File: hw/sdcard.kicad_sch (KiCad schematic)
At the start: 5 parts, among them J2401 MSD-1-A, U2401 CM1624

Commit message: Starting to switch to new rx architecture
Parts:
- renumbered C2401 to C2701, C2402 to C2702, J2401 to J2701, R2401 to R2701, U2401 to U2701
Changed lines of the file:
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@@
 		(dnp no)
 		(fields_autoplaced yes)
-		(property "Reference" "#PWR02401"
+		(property "Reference" "#PWR02701"
 			(at 71.12 102.87 0)
 			(effects
@@
 			(project "USB-SSB-txcvr"
 				(path "/8ae46c04-d01a-4756-8774-512b694bfaff/c32f5700-dc71-4705-afb9-ca83a93b0543/ec3731a3-df09-4e93-b25b-76297aeb30bb"
-					(reference "#PWR02401")
+					(reference "#PWR02701")
 					(unit 1)
 				)
@@
 		(on_board yes)
 		(dnp no)
-		(property "Reference" "U2401"
+		(property "Reference" "U2701"
 			(at 68.9767 57.15 0)
 			(effects
@@
 			(project "USB-SSB-txcvr"
 				(path "/8ae46c04-d01a-4756-8774-512b694bfaff/c32f5700-dc71-4705-afb9-ca83a93b0543/ec3731a3-df09-4e93-b25b-76297aeb30bb"
-					(reference "U2401")
+					(reference "U2701")
 					(unit 1)
 				)
@@
 		(dnp no)
 		(fields_autoplaced yes)
-		(property "Reference" "#PWR02405"
+		(property "Reference" "#PWR02705"
 			(at 185.42 67.31 0)
 			(effects
@@
 			(project ""
 				(path "/8ae46c04-d01a-4756-8774-512b694bfaff/c32f5700-dc71-4705-afb9-ca83a93b0543/ec3731a3-df09-4e93-b25b-76297aeb30bb"
-					(reference "#PWR02405")
+					(reference "#PWR02705")
 					(unit 1)
 				)
@@
 		(dnp no)
 		(fields_autoplaced yes)
-		(property "Reference" "J2401"
+		(property "Reference" "J2701"
 			(at 154.94 63.5 0)
 			(effects
@@
 			(project ""
 				(path "/8ae46c04-d01a-4756-8774-512b694bfaff/c32f5700-dc71-4705-afb9-ca83a93b0543/ec3731a3-df09-4e93-b25b-76297aeb30bb"
-					(reference "J2401")
+					(reference "J2701")
 					(unit 1)
 				)
@@
 		(on_board yes)
 		(dnp no)
-		(property "Reference" "C2402"
+		(property "Reference" "C2702"
 			(at 116.078 78.994 0)
 			(effects
@@
 			(project ""
 				(path "/8ae46c04-d01a-4756-8774-512b694bfaff/c32f5700-dc71-4705-afb9-ca83a93b0543/ec3731a3-df09-4e93-b25b-76297aeb30bb"
-					(reference "C2402")
+					(reference "C2702")
 					(unit 1)
 				)
@@
 		(dnp no)
 		(fields_autoplaced yes)
-		(property "Reference" "#PWR02403"
+		(property "Reference" "#PWR02703"
 			(at 124.46 99.06 0)
 			(effects
@@
 			(project "USB-SSB-txcvr"
 				(path "/8ae46c04-d01a-4756-8774-512b694bfaff/c32f5700-dc71-4705-afb9-ca83a93b0543/ec3731a3-df09-4e93-b25b-76297aeb30bb"
-					(reference "#PWR02403")
+					(reference "#PWR02703")
 					(unit 1)
 				)
@@
 		(on_board yes)
 		(dnp no)
-		(property "Reference" "#PWR02402"
+		(property "Reference" "#PWR02702"
 			(at 124.46 68.58 0)
 			(effects
@@
 			(project "USB-SSB-txcvr"
 				(path "/8ae46c04-d01a-4756-8774-512b694bfaff/c32f5700-dc71-4705-afb9-ca83a93b0543/ec3731a3-df09-4e93-b25b-76297aeb30bb"
-					(reference "#PWR02402")
+					(reference "#PWR02702")
 					(unit 1)
 				)
@@
 		(dnp no)
 		(fields_autoplaced yes)
-		(property "Reference" "#PWR02404"
+		(property "Reference" "#PWR02704"
 			(at 175.26 81.28 0)
 			(effects
@@
 			(project ""
 				(path "/8ae46c04-d01a-4756-8774-512b694bfaff/c32f5700-dc71-4705-afb9-ca83a93b0543/ec3731a3-df09-4e93-b25b-76297aeb30bb"
-					(reference "#PWR02404")
+					(reference "#PWR02704")
 					(unit 1)
 				)
@@
 		(on_board yes)
 		(dnp no)
-		(property "Reference" "C2401"
+		(property "Reference" "C2701"
 			(at 108.458 78.994 0)
 			(effects
@@
 			(project "USB-SSB-txcvr"
 				(path "/8ae46c04-d01a-4756-8774-512b694bfaff/c32f5700-dc71-4705-afb9-ca83a93b0543/ec3731a3-df09-4e93-b25b-76297aeb30bb"
-					(reference "C2401")
+					(reference "C2701")
 					(unit 1)
 				)
@@
 		(dnp no)
 		(fields_autoplaced yes)
-		(property "Reference" "R2401"
+		(property "Reference" "R2701"
 			(at 187.96 77.4699 0)
 			(effects
@@
 			(project ""
 				(path "/8ae46c04-d01a-4756-8774-512b694bfaff/c32f5700-dc71-4705-afb9-ca83a93b0543/ec3731a3-df09-4e93-b25b-76297aeb30bb"
-					(reference "R2401")
+					(reference "R2701")
 					(unit 1)
 				)

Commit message: Converting to use busses as global symbols instead of tedium. Using 2n7002 Nexperia dual MOSFET because of its LOW LOW capacitance spec for L, C, and attenuator switching.
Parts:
- renumbered C2701 to C2401, C2702 to C2402, J2701 to J2401, R2701 to R2401, U2701 to U2401
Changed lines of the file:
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@@
 		(dnp no)
 		(fields_autoplaced yes)
-		(property "Reference" "#PWR02701"
+		(property "Reference" "#PWR02401"
 			(at 71.12 102.87 0)
 			(effects
@@
 					(size 1.27 1.27)
 				)
+				(hide yes)
 			)
 		)
@@
 			(project "USB-SSB-txcvr"
 				(path "/8ae46c04-d01a-4756-8774-512b694bfaff/c32f5700-dc71-4705-afb9-ca83a93b0543/ec3731a3-df09-4e93-b25b-76297aeb30bb"
-					(reference "#PWR02701")
+					(reference "#PWR02401")
 					(unit 1)
 				)
@@
 		(on_board yes)
 		(dnp no)
-		(property "Reference" "U2701"
+		(property "Reference" "U2401"
 			(at 68.9767 57.15 0)
 			(effects
@@
 			(project "USB-SSB-txcvr"
 				(path "/8ae46c04-d01a-4756-8774-512b694bfaff/c32f5700-dc71-4705-afb9-ca83a93b0543/ec3731a3-df09-4e93-b25b-76297aeb30bb"
-					(reference "U2701")
+					(reference "U2401")
 					(unit 1)
 				)
@@
 		(dnp no)
 		(fields_autoplaced yes)
-		(property "Reference" "#PWR02705"
+		(property "Reference" "#PWR02405"
 			(at 185.42 67.31 0)
 			(effects
@@
 			(project ""
 				(path "/8ae46c04-d01a-4756-8774-512b694bfaff/c32f5700-dc71-4705-afb9-ca83a93b0543/ec3731a3-df09-4e93-b25b-76297aeb30bb"
-					(reference "#PWR02705")
+					(reference "#PWR02405")
 					(unit 1)
 				)
@@
 		(dnp no)
 		(fields_autoplaced yes)
-		(property "Reference" "J2701"
+		(property "Reference" "J2401"
 			(at 154.94 63.5 0)
 			(effects
@@
 			(project ""
 				(path "/8ae46c04-d01a-4756-8774-512b694bfaff/c32f5700-dc71-4705-afb9-ca83a93b0543/ec3731a3-df09-4e93-b25b-76297aeb30bb"
-					(reference "J2701")
+					(reference "J2401")
 					(unit 1)
 				)
@@
 		(on_board yes)
 		(dnp no)
-		(property "Reference" "C2702"
+		(property "Reference" "C2402"
 			(at 116.078 78.994 0)
 			(effects
@@
 			(project ""
 				(path "/8ae46c04-d01a-4756-8774-512b694bfaff/c32f5700-dc71-4705-afb9-ca83a93b0543/ec3731a3-df09-4e93-b25b-76297aeb30bb"
-					(reference "C2702")
+					(reference "C2402")
 					(unit 1)
 				)
@@
 		(dnp no)
 		(fields_autoplaced yes)
-		(property "Reference" "#PWR02703"
+		(property "Reference" "#PWR02403"
 			(at 124.46 99.06 0)
 			(effects
@@
 					(size 1.27 1.27)
 				)
+				(hide yes)
 			)
 		)
@@
 			(project "USB-SSB-txcvr"
 				(path "/8ae46c04-d01a-4756-8774-512b694bfaff/c32f5700-dc71-4705-afb9-ca83a93b0543/ec3731a3-df09-4e93-b25b-76297aeb30bb"
-					(reference "#PWR02703")
+					(reference "#PWR02403")
 					(unit 1)
 				)
@@
 		(on_board yes)
 		(dnp no)
-		(property "Reference" "#PWR02702"
+		(property "Reference" "#PWR02402"
 			(at 124.46 68.58 0)
 			(effects
@@
 			(project "USB-SSB-txcvr"
 				(path "/8ae46c04-d01a-4756-8774-512b694bfaff/c32f5700-dc71-4705-afb9-ca83a93b0543/ec3731a3-df09-4e93-b25b-76297aeb30bb"
-					(reference "#PWR02702")
+					(reference "#PWR02402")
 					(unit 1)
 				)
@@
 		(dnp no)
 		(fields_autoplaced yes)
-		(property "Reference" "#PWR02704"
+		(property "Reference" "#PWR02404"
 			(at 175.26 81.28 0)
 			(effects
@@
 			(project ""
 				(path "/8ae46c04-d01a-4756-8774-512b694bfaff/c32f5700-dc71-4705-afb9-ca83a93b0543/ec3731a3-df09-4e93-b25b-76297aeb30bb"
-					(reference "#PWR02704")
+					(reference "#PWR02404")
 					(unit 1)
 				)
@@
 		(on_board yes)
 		(dnp no)
-		(property "Reference" "C2701"
+		(property "Reference" "C2401"
 			(at 108.458 78.994 0)
 			(effects
@@
 			(project "USB-SSB-txcvr"
 				(path "/8ae46c04-d01a-4756-8774-512b694bfaff/c32f5700-dc71-4705-afb9-ca83a93b0543/ec3731a3-df09-4e93-b25b-76297aeb30bb"
-					(reference "C2701")
+					(reference "C2401")
 					(unit 1)
 				)
@@
 		(dnp no)
 		(fields_autoplaced yes)
-		(property "Reference" "R2701"
+		(property "Reference" "R2401"
 			(at 187.96 77.4699 0)
 			(effects
@@
 			(project ""
 				(path "/8ae46c04-d01a-4756-8774-512b694bfaff/c32f5700-dc71-4705-afb9-ca83a93b0543/ec3731a3-df09-4e93-b25b-76297aeb30bb"
-					(reference "R2701")
+					(reference "R2401")
 					(unit 1)
 				)

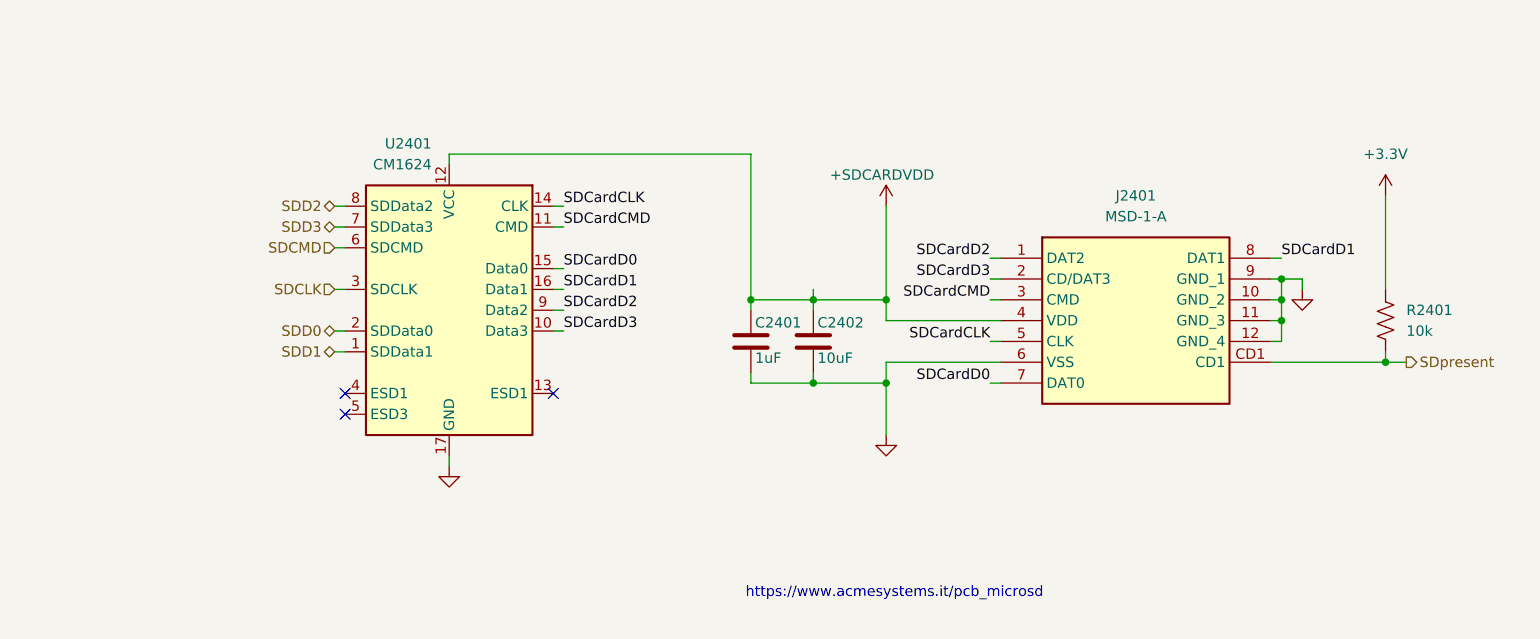
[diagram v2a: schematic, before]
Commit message: Added SD card ESD zap
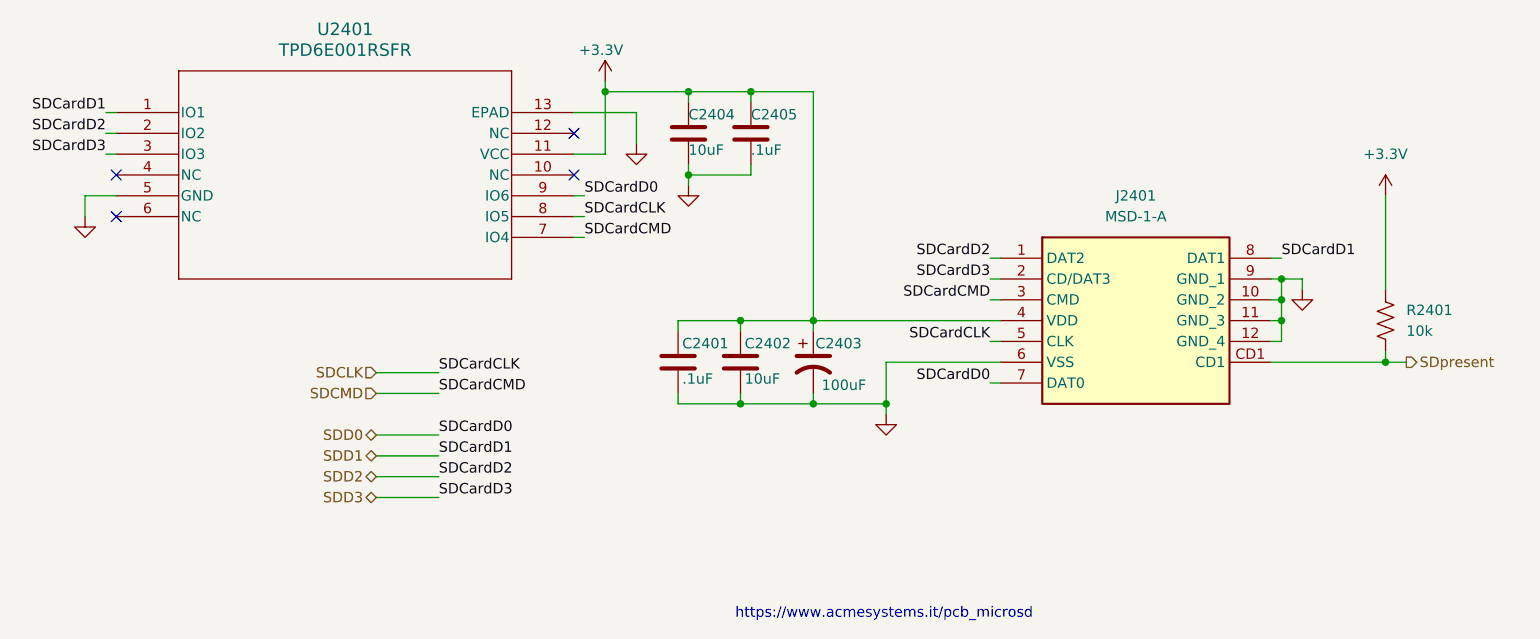
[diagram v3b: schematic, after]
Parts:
- removed U2401: CM1624, Package_DFN_QFN:OnSemi_UDFN-16-1EP_1.35x3.3mm_P0.4mm_EP0.4x2.8mm, symbol Power_Protection:CM1624
- added C2403: 100uF, symbol Device:C_Polarized_US
- added C2404: 10uF, Capacitor_SMD:C_0805_2012Metric, symbol Device:C
- added C2405: .1uF, Capacitor_SMD:C_0805_2012Metric, symbol Device:C
- added U2401: TPD6E001RSFR, RSF12_2P1X2P1, symbol TPD6E001RSFR:TPD6E001RSFR
- C2401: value 1uF -> .1uF
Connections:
- net +SDCARDVDD is gone; now on net +3.3V: C2401.1, C2402.1, J2401.4 (VDD)
- net SDCardCLK is gone; now on net SDCLK: J2401.5 (CLK)
- net SDCardCMD is gone; now on net SDCMD: J2401.3 (CMD)
- net SDCardD0 is gone; now on net SDD0: J2401.7 (DAT0)
- net SDCardD1 is gone; now on net SDD1: J2401.8 (DAT1)
- net SDCardD2 is gone; now on net SDD2: J2401.1 (DAT2)
- net SDCardD3 is gone; now on net SDD3: J2401.2 (CD/DAT3)
- net +3.3V: now also C2403.1, C2404.1, C2405.1, U2401.11 (VCC)
- net GND: now also C2403.2, C2404.2, C2405.2, U2401.13 (EPAD), U2401.5 (GND)
- net SDCLK: now also U2401.8 (IO5)
- net SDCMD: now also U2401.7 (IO4)
- net SDD0: now also U2401.9 (IO6)
- net SDD1: now also U2401.1 (IO1)
- net SDD2: now also U2401.2 (IO2)
- net SDD3: now also U2401.3 (IO3)
- no-connect marks 3 -> 4
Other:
- moved on the sheet: C2401, C2402

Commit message: Moved ant page into tx page, added Bruene Direction Coupler to measure VSWR. General cleanup, page renumber, reannote
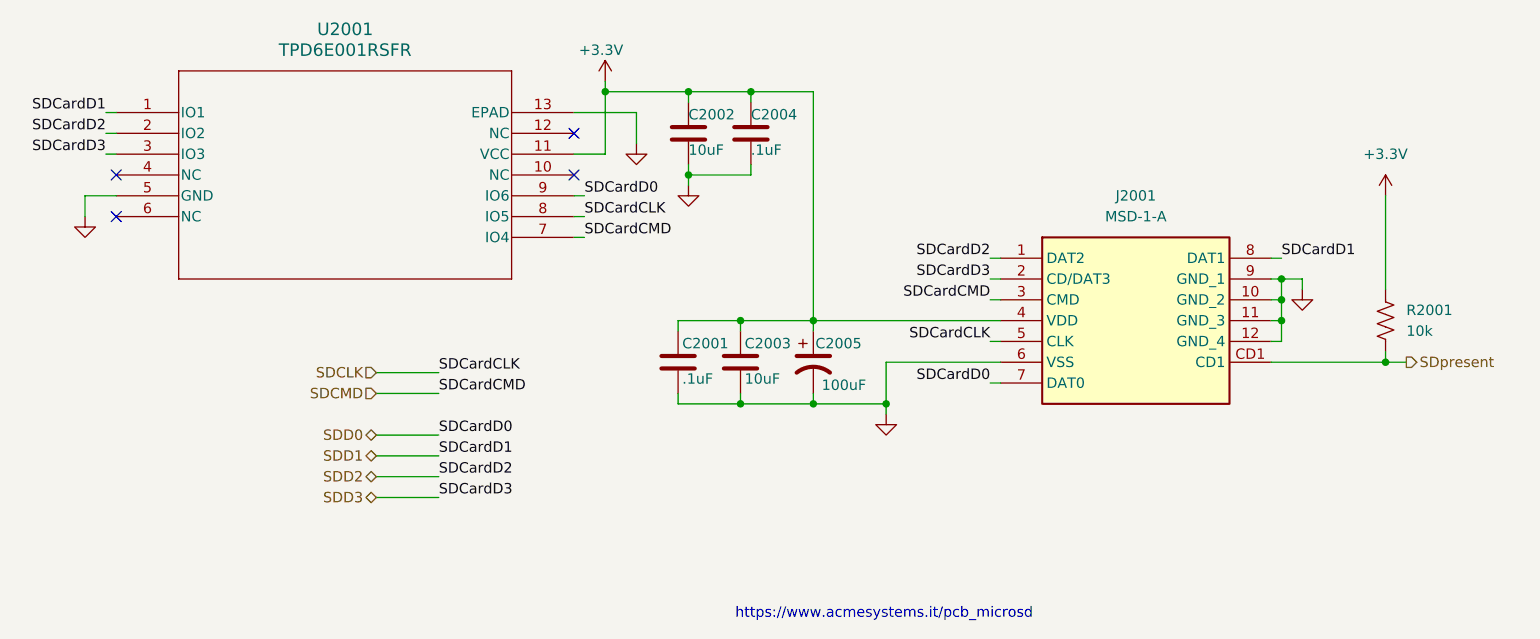
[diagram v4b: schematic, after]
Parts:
- renumbered C2401 to C2001, C2404 to C2002, C2402 to C2003, C2405 to C2004, C2403 to C2005, J2401 to J2001, R2401 to R2001, U2401 to U2001
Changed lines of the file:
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@@
 		(dnp no)
 		(fields_autoplaced yes)
-		(property "Reference" "#PWR02401"
+		(property "Reference" "#PWR02001"
 			(at 26.67 72.39 0)
 			(effects
@@
 			(project "USB-SSB-txcvr"
 				(path "/8ae46c04-d01a-4756-8774-512b694bfaff/c32f5700-dc71-4705-afb9-ca83a93b0543/ec3731a3-df09-4e93-b25b-76297aeb30bb"
-					(reference "#PWR02401")
+					(reference "#PWR02001")
 					(unit 1)
 				)
@@
 		(dnp no)
 		(fields_autoplaced yes)
-		(property "Reference" "#PWR02405"
+		(property "Reference" "#PWR02007"
 			(at 185.42 67.31 0)
 			(effects
@@
 			(project ""
 				(path "/8ae46c04-d01a-4756-8774-512b694bfaff/c32f5700-dc71-4705-afb9-ca83a93b0543/ec3731a3-df09-4e93-b25b-76297aeb30bb"
-					(reference "#PWR02405")
+					(reference "#PWR02007")
 					(unit 1)
 				)
@@
 		(on_board yes)
 		(dnp no)
-		(property "Reference" "#PWR02407"
+		(property "Reference" "#PWR02002"
 			(at 90.17 53.34 0)
 			(effects
@@
 			(project "USB-SSB-txcvr"
 				(path "/8ae46c04-d01a-4756-8774-512b694bfaff/c32f5700-dc71-4705-afb9-ca83a93b0543/ec3731a3-df09-4e93-b25b-76297aeb30bb"
-					(reference "#PWR02407")
+					(reference "#PWR02002")
 					(unit 1)
 				)
@@
 		(dnp no)
 		(fields_autoplaced yes)
-		(property "Reference" "U2401"
+		(property "Reference" "U2001"
 			(at 58.42 43.18 0)
 			(effects
@@
 			(project ""
 				(path "/8ae46c04-d01a-4756-8774-512b694bfaff/c32f5700-dc71-4705-afb9-ca83a93b0543/ec3731a3-df09-4e93-b25b-76297aeb30bb"
-					(reference "U2401")
+					(reference "U2001")
 					(unit 1)
 				)
@@
 		(on_board yes)
 		(dnp no)
-		(property "Reference" "C2404"
+		(property "Reference" "C2002"
 			(at 100.33 53.594 0)
 			(effects
@@
 			(project "USB-SSB-txcvr"
 				(path "/8ae46c04-d01a-4756-8774-512b694bfaff/c32f5700-dc71-4705-afb9-ca83a93b0543/ec3731a3-df09-4e93-b25b-76297aeb30bb"
-					(reference "C2404")
+					(reference "C2002")
 					(unit 1)
 				)
@@
 		(dnp no)
 		(fields_autoplaced yes)
-		(property "Reference" "#PWR02406"
+		(property "Reference" "#PWR02003"
 			(at 93.98 63.5 0)
 			(effects
@@
 			(project "USB-SSB-txcvr"
 				(path "/8ae46c04-d01a-4756-8774-512b694bfaff/c32f5700-dc71-4705-afb9-ca83a93b0543/ec3731a3-df09-4e93-b25b-76297aeb30bb"
-					(reference "#PWR02406")
+					(reference "#PWR02003")
 					(unit 1)
 				)
@@
 		(dnp no)
 		(fields_autoplaced yes)
-		(property "Reference" "J2401"
+		(property "Reference" "J2001"
 			(at 154.94 63.5 0)
 			(effects
@@
 			(project ""
 				(path "/8ae46c04-d01a-4756-8774-512b694bfaff/c32f5700-dc71-4705-afb9-ca83a93b0543/ec3731a3-df09-4e93-b25b-76297aeb30bb"
-					(reference "J2401")
+					(reference "J2001")
 					(unit 1)
 				)
@@
 		(dnp no)
 		(fields_autoplaced yes)
-		(property "Reference" "#PWR02408"
+		(property "Reference" "#PWR02004"
 			(at 100.33 68.58 0)
 			(effects
@@
 			(project "USB-SSB-txcvr"
 				(path "/8ae46c04-d01a-4756-8774-512b694bfaff/c32f5700-dc71-4705-afb9-ca83a93b0543/ec3731a3-df09-4e93-b25b-76297aeb30bb"
-					(reference "#PWR02408")
+					(reference "#PWR02004")
 					(unit 1)
 				)
@@
 		(on_board yes)
 		(dnp no)
-		(property "Reference" "C2402"
+		(property "Reference" "C2003"
 			(at 107.188 81.534 0)
 			(effects
@@
 			(project ""
 				(path "/8ae46c04-d01a-4756-8774-512b694bfaff/c32f5700-dc71-4705-afb9-ca83a93b0543/ec3731a3-df09-4e93-b25b-76297aeb30bb"
-					(reference "C2402")
+					(reference "C2003")
 					(unit 1)
 				)
@@
 		(dnp no)
 		(fields_autoplaced yes)
-		(property "Reference" "#PWR02403"
+		(property "Reference" "#PWR02005"
 			(at 124.46 96.52 0)
 			(effects
@@
 			(project "USB-SSB-txcvr"
 				(path "/8ae46c04-d01a-4756-8774-512b694bfaff/c32f5700-dc71-4705-afb9-ca83a93b0543/ec3731a3-df09-4e93-b25b-76297aeb30bb"
-					(reference "#PWR02403")
+					(reference "#PWR02005")
 					(unit 1)
 				)
@@
 		(dnp no)
 		(fields_autoplaced yes)
-		(property "Reference" "#PWR02404"
+		(property "Reference" "#PWR02006"
 			(at 175.26 81.28 0)
 			(effects
@@
 			(project ""
 				(path "/8ae46c04-d01a-4756-8774-512b694bfaff/c32f5700-dc71-4705-afb9-ca83a93b0543/ec3731a3-df09-4e93-b25b-76297aeb30bb"
-					(reference "#PWR02404")
+					(reference "#PWR02006")
 					(unit 1)
 				)
@@
 		(on_board yes)
 		(dnp no)
-		(property "Reference" "C2403"
+		(property "Reference" "C2005"
 			(at 115.824 81.534 0)
 			(effects
@@
 			(project ""
 				(path "/8ae46c04-d01a-4756-8774-512b694bfaff/c32f5700-dc71-4705-afb9-ca83a93b0543/ec3731a3-df09-4e93-b25b-76297aeb30bb"
-					(reference "C2403")
+					(reference "C2005")
 					(unit 1)
 				)
@@
 		(on_board yes)
 		(dnp no)
-		(property "Reference" "C2401"
+		(property "Reference" "C2001"
 			(at 99.568 81.534 0)
 			(effects
@@
 			(project "USB-SSB-txcvr"
 				(path "/8ae46c04-d01a-4756-8774-512b694bfaff/c32f5700-dc71-4705-afb9-ca83a93b0543/ec3731a3-df09-4e93-b25b-76297aeb30bb"
-					(reference "C2401")
+					(reference "C2001")
 					(unit 1)
 				)
@@
 		(on_board yes)
 		(dnp no)
-		(property "Reference" "C2405"
+		(property "Reference" "C2004"
 			(at 107.95 53.594 0)
 			(effects
@@
 			(project "USB-SSB-txcvr"
 				(path "/8ae46c04-d01a-4756-8774-512b694bfaff/c32f5700-dc71-4705-afb9-ca83a93b0543/ec3731a3-df09-4e93-b25b-76297aeb30bb"
-					(reference "C2405")
+					(reference "C2004")
 					(unit 1)
 				)
@@
 		(dnp no)
 		(fields_autoplaced yes)
-		(property "Reference" "R2401"
+		(property "Reference" "R2001"
 			(at 187.96 77.4699 0)
 			(effects
@@
 			(project ""
 				(path "/8ae46c04-d01a-4756-8774-512b694bfaff/c32f5700-dc71-4705-afb9-ca83a93b0543/ec3731a3-df09-4e93-b25b-76297aeb30bb"
-					(reference "R2401")
-					(unit 1)
-				)
+					(reference "R2001")
+					(unit 1)
+				)

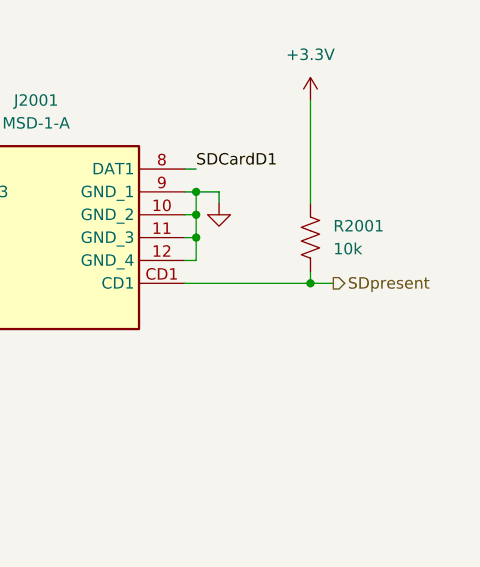
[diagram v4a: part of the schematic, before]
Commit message: Working on QSD, PGA, audio codec input path
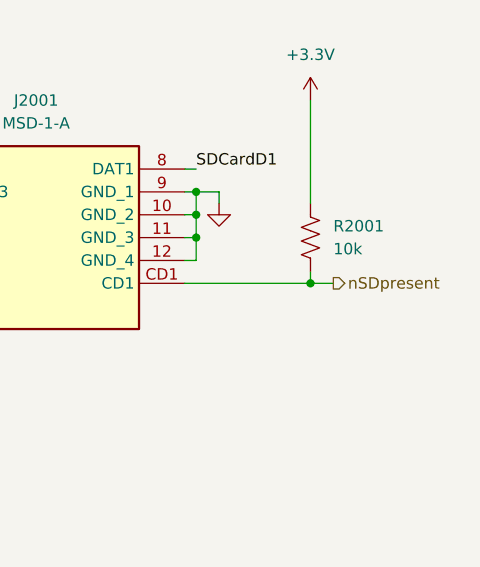
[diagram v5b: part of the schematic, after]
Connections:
- net SDpresent renamed nSDpresent
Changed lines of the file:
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@@
 		)
 	)
-	(hierarchical_label "SDpresent"
+	(hierarchical_label "nSDpresent"
 		(shape output)
 		(at 187.96 83.82 0)
